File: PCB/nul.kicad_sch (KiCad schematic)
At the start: 22 parts, among them J1 Conn_Coaxial, U1 ESP32-C3FH4, Y1 40MHz

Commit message: add ldo, led, and other parts
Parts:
- added C11, C12: 10uf, symbol Device:C
- added J2: LED Socket, symbol Connector:Conn_01x03_Socket
- added U2: AMS1117-3.3, Package_TO_SOT_SMD:SOT-223-3_TabPin2, symbol Regulator_Linear:AMS1117-3.3
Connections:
- net +3.3V: now also C12.1, J2.1 (Pin_1), U2.2 (VO)
- net GND: now also C11.2, C12.2, J2.3 (Pin_3), U2.1 (GND)
- net LED: now also J2.2 (Pin_2)
- new net +5V: C11.1, U2.3 (VI)
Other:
- note added: "ESP"
- note added: "LDO"
- note added: "LED"

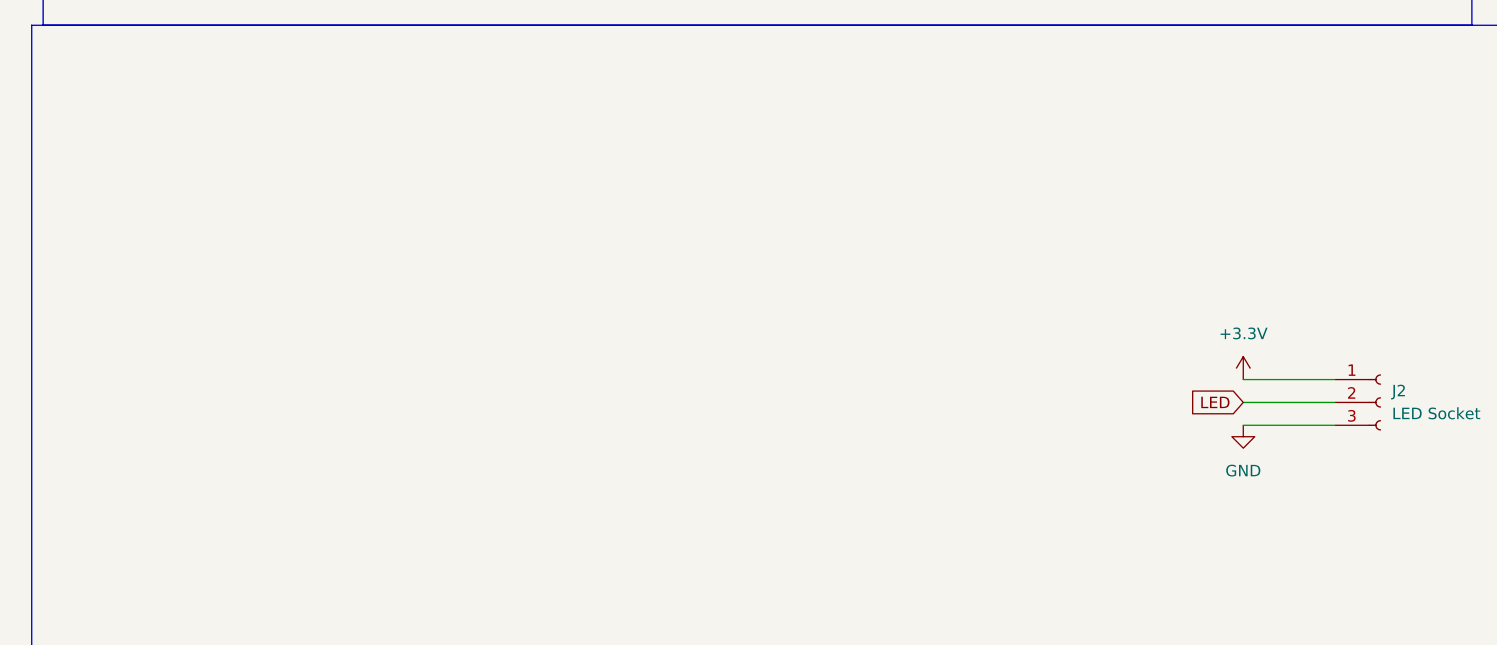
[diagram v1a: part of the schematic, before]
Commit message: Finish schematic
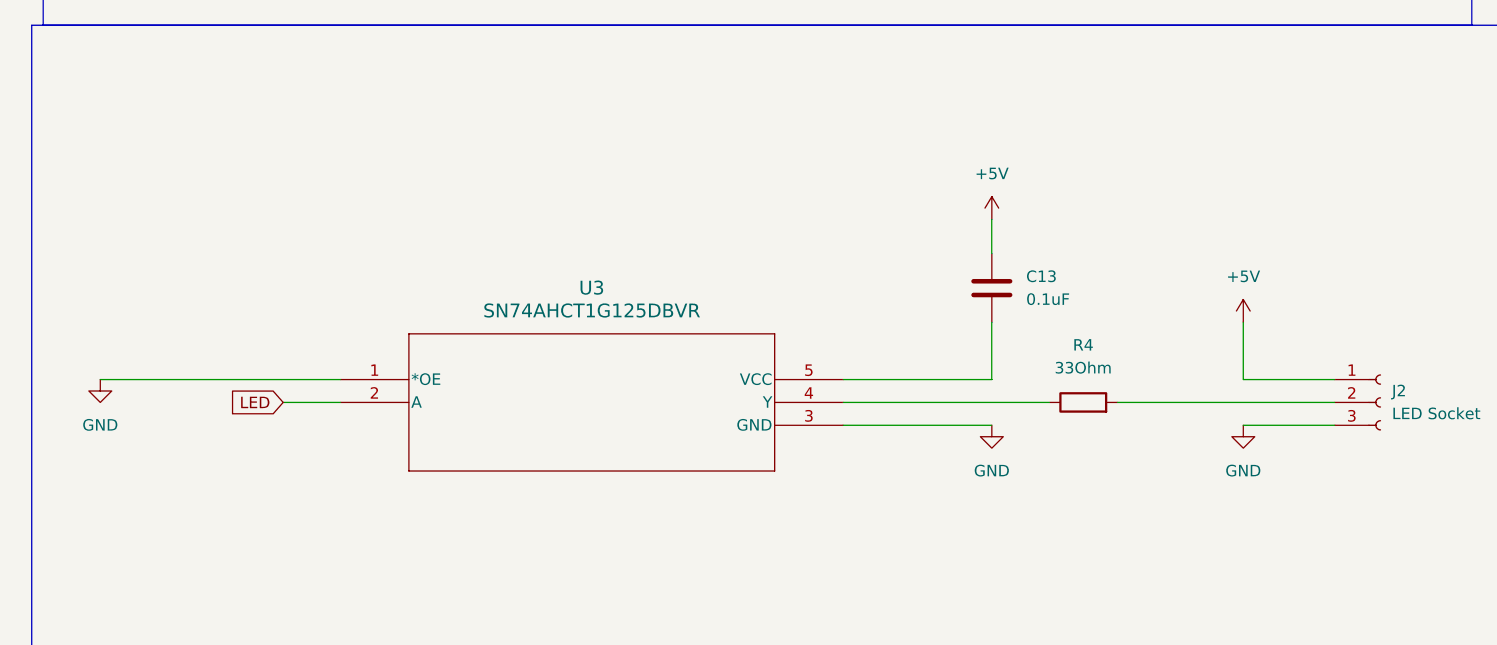
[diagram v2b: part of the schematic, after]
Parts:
- added C13: 0.1uF, symbol Device:C
- added R4: 33Ohm, symbol Device:R
- added U3: SN74AHCT1G125DBVR, DBV5, symbol SN74AHCT1G125DBVR:SN74AHCT1G125DBVR
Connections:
- net +3.3V: no longer J2.1 (Pin_1)
- net +5V: now also J2.1 (Pin_1), C13.1
- net GND: now also U3.1 (*OE), U3.3 (GND)
- net LED: now also U3.2 (A); no longer J2.2 (Pin_2)
- new net: J2.2 (Pin_2), R4.2
- new net: R4.1, U3.4 (Y)
- new net: C13.2, U3.5 (VCC)

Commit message: footprints
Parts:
- removed J1: Conn_Coaxial, symbol Connector:Conn_Coaxial
- removed Y1: 40MHz, symbol Device:Crystal
- added JP2: U.FL-R-SMT-1, easyeda2kicad:RF-SMD_FRF05002-JSS103M, symbol easyeda2kicad:U.FL-R-SMT-1
- added R5, R6: 5.1k, Resistor_SMD:R_0402_1005Metric, symbol Device:R
- added R7: 10k, Resistor_SMD:R_0402_1005Metric, symbol Device:R
- added U4: XRCGB40M000F1S1DR0, easyeda2kicad:CRYSTAL-SMD_4P-L2.0-W1.6-BL, symbol easyeda2kicad:XRCGB40M000F1S1DR0
- added USBC1: FUC-24F11-SNLB1, easyeda2kicad:USB-C-SMD_C67380, symbol easyeda2kicad:FUC-24F11-SNLB1
- C1, C10, C11, C12, C13, C2, C3, C4, C5, C6, C7, C8, C9: footprint (none) -> Capacitor_SMD:C_0402_1005Metric
- J2: footprint (none) -> Connector_PinHeader_2.54mm:PinHeader_1x03_P2.54mm_Vertical_SMD_Pin1Left
- JP1: footprint (none) -> Jumper:SolderJumper-2_P1.3mm_Open_RoundedPad1.0x1.5mm
- L1, L2: footprint (none) -> Inductor_SMD:L_0402_1005Metric
- R1, R2, R3, R4: footprint (none) -> Resistor_SMD:R_0402_1005Metric
- TP1, TP2, TP3: footprint (none) -> TestPoint:TestPoint_Pad_D1.5mm
- U3: footprint DBV5 -> SN74AHCT1G125DBVR:DBV5
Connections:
- net +3.3V: now also R7.1
- net +5V: now also USBC1.A4 (VBUS), USBC1.A9 (VBUS), USBC1.B4 (VBUS), USBC1.B9 (VBUS)
- net GND: now also JP2.2 (GND), JP2.3 (GND), R5.1, R6.1, USBC1.13 (EP), USBC1.14 (EP), USBC1.15 (EP), USBC1.16 (EP), USBC1.A1 (GND), USBC1.A12 (GND), USBC1.B1 (GND), USBC1.B12 (GND)
- net USB_D+: now also USBC1.A6 (DP1), USBC1.B6 (DP2)
- net USB_D-: now also USBC1.A7 (DN1), USBC1.B7 (DN2)
- net at C10.1, L1.1: now also JP2.1 (SIG)
- net at C8.2, L2.2: now also U4.1
- net at C7.1, U1.29 (XTAL_N): now also U4.3
- net at JP1.1 (A), U1.15 (GPIO9): now also R7.2
- new net: R6.2, USBC1.B5 (CC2)
- new net: R5.2, USBC1.A5 (CC1)
- no-connect marks 14 -> 26
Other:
- note added: "USB"

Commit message: sanity check schematic & update
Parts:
- removed L2: 15nH, 300ma, Inductor_SMD:L_0402_1005Metric, symbol Device:L
- added C14: 220uf, Capacitor_SMD:C_1210_3225Metric, symbol Device:C
- added R8, R9: 33Ohm, Resistor_SMD:R_0402_1005Metric, symbol Device:R
- added U5: SRV05-4, Package_TO_SOT_SMD:SOT-23-6, symbol Power_Protection:SRV05-4
- C1, C13, C2, C3, C4, C5: LCSC Part (none) -> C1525
- C10, C9: LCSC Part (none) -> C1552
- C6: LCSC Part (none) -> C52923
- C7, C8: LCSC Part (none) -> C1548
- L1: LCSC Part (none) -> C27122
- R1, R2, R3, R7: LCSC Part (none) -> C25744
- R4: LCSC Part (none) -> C25105
- R5, R6: LCSC Part (none) -> C25905
- U2: LCSC Part (none) -> C6186
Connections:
- net +5V: now also C14.1, U5.5 (VP)
- net GND: now also C14.2, U5.2 (VN)
- net USB_D+: now also R9.2, U5.1 (IO1); no longer U1.26 (GPIO19/USB_D+)
- net USB_D-: now also R8.2, U5.3 (IO2); no longer U1.25 (GPIO18/USB_D-)
- net at C8.2, U4.1: now also U1.30 (XTAL_P)
- new net: R8.1, U1.25 (GPIO18/USB_D-)
- new net: R9.1, U1.26 (GPIO19/USB_D+)
- no-connect marks 26 -> 28
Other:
- note added: "POWER"
- note removed: "LDO"
- moved on the sheet: C11, C12, R5, R6, U2, USBC1

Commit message: pcb layout
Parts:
- J2: footprint Connector_PinHeader_2.54mm:PinHeader_1x03_P2.54mm_Vertical_SMD_Pin1Left -> Connector_PinHeader_2.54mm:PinHeader_1x03_P2.54mm_Vertical
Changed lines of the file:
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@@
 			)
 		)
-		(property "Footprint" "Connector_PinHeader_2.54mm:PinHeader_1x03_P2.54mm_Vertical_SMD_Pin1Left"
+		(property "Footprint" "Connector_PinHeader_2.54mm:PinHeader_1x03_P2.54mm_Vertical"
 			(at 161.29 156.21 0)
 			(hide yes)

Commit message: pcb v1
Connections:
- net USB_DATA+: now reaches R8.1, U1.25 (GPIO18/USB_D-)
- net USB_DATA-: now reaches R9.1, U1.26 (GPIO19/USB_D+)
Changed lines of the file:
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@@
+		)
+	)
+	(label "USB_DATA-"
+		(at 124.46 83.82 0)
+		(effects
+			(font
+				(size 1.27 1.27)
+			)
+			(justify left bottom)
+		)
+	)
+	(label "USB_DATA+"
+		(at 130.81 81.28 90)
+		(effects
+			(font
+				(size 1.27 1.27)
+			)
+			(justify left bottom)
 		)
 	)

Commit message: fix decop cap schematic
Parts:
- removed C13: 0.1uF, Capacitor_SMD:C_0402_1005Metric, symbol Device:C
- added C13: 0.1uF ceramic, Capacitor_SMD:C_0402_1005Metric, symbol Device:C_Small
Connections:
- net +5V: now also U3.5 (VCC), C13.2
- net GND: now also C13.1
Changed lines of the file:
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@@
 	)
 	(junction
+		(at 107.95 153.67)
+		(diameter 0)
+		(color 0 0 0 0)
+	)
+	(junction
 		(at 149.86 24.13)
 		(diameter 0)
@@
 	(wire
 		(pts
-			(xy 101.6 153.67) (xy 118.11 153.67)
+			(xy 101.6 153.67) (xy 107.95 153.67)
 		)
 		(stroke
@@
 	(wire
 		(pts
-			(xy 118.11 135.89) (xy 118.11 139.7)
-		)
-		(stroke
-			(width 0)
-			(type default)
-		)
-	)
-	(wire
-		(pts
 			(xy 19.05 153.67) (xy 45.72 153.67)
 		)
@@
 	(wire
 		(pts
+			(xy 107.95 153.67) (xy 118.11 153.67)
+		)
+		(stroke
+			(width 0)
+			(type default)
+		)
+	)
+	(wire
+		(pts
 			(xy 160.02 55.88) (xy 163.83 55.88)
 		)
@@
 	(wire
 		(pts
+			(xy 107.95 148.59) (xy 107.95 146.05)
+		)
+		(stroke
+			(width 0)
+			(type default)
+		)
+	)
+	(wire
+		(pts
 			(xy 132.08 43.18) (xy 134.62 43.18)
 		)
@@
 	(symbol
 		(lib_id "power:GND")
+		(at 107.95 146.05 180)
+		(unit 1)
+		(body_style 1)
+		(exclude_from_sim no)
+		(in_bom yes)
+		(on_board yes)
+		(in_pos_files yes)
+		(dnp no)
+		(fields_autoplaced yes)
+		(property "Reference" "#PWR042"
+			(at 107.95 139.7 0)
+			(hide yes)
+			(show_name no)
+			(do_not_autoplace no)
+			(effects
+				(font
+					(size 1.27 1.27)
+				)
+			)
+		)
+		(property "Value" "GND"
+			(at 107.95 140.97 0)
+			(show_name no)
+			(do_not_autoplace no)
+			(effects
+				(font
+					(size 1.27 1.27)
+				)
+			)
+		)
+		(property "Footprint" ""
+			(at 107.95 146.05 0)
+			(hide yes)
+			(show_name no)
+			(do_not_autoplace no)
+			(effects
+				(font
+					(size 1.27 1.27)
+				)
+			)
+		)
+		(property "Datasheet" ""
+			(at 107.95 146.05 0)
+			(hide yes)
+			(show_name no)
+			(do_not_autoplace no)
+			(effects
+				(font
+					(size 1.27 1.27)
+				)
+			)
+		)
+		(property "Description" "Power symbol creates a global label with name \"GND\" , ground"
+			(at 107.95 146.05 0)
+			(hide yes)
+			(show_name no)
+			(do_not_autoplace no)
+			(effects
+				(font
+					(size 1.27 1.27)
+				)
+			)
+		)
+		(pin "1"
+		)
+		(instances
+			(project "nul"
+				(path "/fd672162-7b7f-4b25-941f-c6fc959beb48"
+					(reference "#PWR042")
+					(unit 1)
+				)
+			)
+		)
+	)
+	(symbol
+		(lib_id "power:GND")
 		(at 146.05 158.75 0)
 		(unit 1)
@@
 	)
 	(symbol
+		(lib_id "Device:C_Small")
+		(at 107.95 151.13 0)
+		(unit 1)
+		(body_style 1)
+		(exclude_from_sim no)
+		(in_bom yes)
+		(on_board yes)
+		(in_pos_files yes)
+		(dnp no)
+		(property "Reference" "C13"
+			(at 108.966 148.336 90)
+			(show_name no)
+			(do_not_autoplace no)
+			(effects
+				(font
+					(size 1.27 1.27)
+				)
+			)
+		)
+		(property "Value" "0.1uF ceramic"
+			(at 111.76 151.1363 90)
+			(hide yes)
+			(show_name no)
+			(do_not_autoplace no)
+			(effects
+				(font
+					(size 1.27 1.27)
+				)
+			)
+		)
+		(property "Footprint" "Capacitor_SMD:C_0402_1005Metric"
+			(at 107.95 151.13 0)
+			(hide yes)
+			(show_name no)
+			(do_not_autoplace no)
+			(effects
+				(font
+					(size 1.27 1.27)
+				)
+			)
+		)
+		(property "Datasheet" ""
+			(at 107.95 151.13 0)
+			(hide yes)
+			(show_name no)
+			(do_not_autoplace no)
+			(effects
+				(font
+					(size 1.27 1.27)
+				)
+			)
+		)
+		(property "Description" "Unpolarized capacitor, small symbol"
+			(at 107.95 151.13 0)
+			(hide yes)
+			(show_name no)
+			(do_not_autoplace no)
+			(effects
+				(font
+					(size 1.27 1.27)
+				)
+			)
+		)
+		(property "LCSC Part" "C1525"
+			(at 107.95 151.13 90)
+			(hide yes)
+			(show_name no)
+			(do_not_autoplace no)
+			(effects
+				(font
+					(size 1.27 1.27)
+				)
+			)
+		)
+		(pin "1"
+		)
+		(pin "2"
+		)
+		(instances
+			(project "nul"
+				(path "/fd672162-7b7f-4b25-941f-c6fc959beb48"
+					(reference "C13")
+					(unit 1)
+				)
+			)
+		)
+	)
+	(symbol
 		(lib_id "power:+5V")
 		(at 261.62 147.32 0)
@@
 	(symbol
 		(lib_id "power:+5V")
-		(at 118.11 135.89 0)
+		(at 118.11 147.32 0)
 		(unit 1)
 		(body_style 1)
@@
 		(fields_autoplaced yes)
 		(property "Reference" "#PWR024"
-			(at 118.11 139.7 0)
+			(at 118.11 151.13 0)
 			(hide yes)
 			(show_name no)
@@
 		)
 		(property "Value" "+5V"
-			(at 118.11 130.81 0)
+			(at 118.11 142.24 0)
 			(show_name no)
 			(do_not_autoplace no)
@@
 		)
 		(property "Footprint" ""
-			(at 118.11 135.89 0)
+			(at 118.11 147.32 0)
 			(hide yes)
 			(show_name no)
@@
 		)
 		(property "Datasheet" ""
-			(at 118.11 135.89 0)
+			(at 118.11 147.32 0)
 			(hide yes)
 			(show_name no)
@@
 		)
 		(property "Description" "Power symbol creates a global label with name \"+5V\""
-			(at 118.11 135.89 0)
+			(at 118.11 147.32 0)
 			(hide yes)
 			(show_name no)
@@
 					(unit 1)
 				)
-			)
-		)
-	)
-	(symbol
-		(lib_id "Device:C")
-		(at 118.11 143.51 0)
-		(unit 1)
-		(body_style 1)
-		(exclude_from_sim no)
-		(in_bom yes)
-		(on_board yes)
-		(in_pos_files yes)
-		(dnp no)
-		(fields_autoplaced yes)
-		(property "Reference" "C13"
-			(at 121.92 142.2399 0)
-			(show_name no)
-			(do_not_autoplace no)
-			(effects
-				(font
-					(size 1.27 1.27)
-				)
-				(justify left)
-			)
-		)
-		(property "Value" "0.1uF"
-			(at 121.92 144.7799 0)
-			(show_name no)
-			(do_not_autoplace no)
-			(effects
-				(font
-					(size 1.27 1.27)
-				)
-				(justify left)
-			)
-		)
-		(property "Footprint" "Capacitor_SMD:C_0402_1005Metric"
-			(at 119.0752 147.32 0)
-			(hide yes)
-			(show_name no)
-			(do_not_autoplace no)
-			(effects
-				(font
-					(size 1.27 1.27)
-				)
-			)
-		)
-		(property "Datasheet" ""
-			(at 118.11 143.51 0)
-			(hide yes)
-			(show_name no)
-			(do_not_autoplace no)
-			(effects
-				(font
-					(size 1.27 1.27)
-				)
-			)
-		)
-		(property "Description" "Unpolarized capacitor"
-			(at 118.11 143.51 0)
-			(hide yes)
-			(show_name no)
-			(do_not_autoplace no)
-			(effects
-				(font
-					(size 1.27 1.27)
-				)
-			)
-		)
-		(property "LCSC Part" "C1525"
-			(at 118.11 143.51 0)
-			(hide yes)
-			(show_name no)
-			(do_not_autoplace no)
-			(effects
-				(font
-					(size 1.27 1.27)
-				)
-			)
-		)
-		(pin "2"
-		)
-		(pin "1"
-		)
-		(instances
-			(project "nul"
-				(path "/fd672162-7b7f-4b25-941f-c6fc959beb48"
-					(reference "C13")
-					(unit 1)
-				)
